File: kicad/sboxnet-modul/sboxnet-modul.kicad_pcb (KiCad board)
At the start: 2 copper layers, 67.3 x 62.2 mm, 38 parts, among them J1 Conn_01x03, J2 Conn_01x04, J4 8P8C, J5 8P8C, J6 sboxnet-buchse_2x17, SW1 SW_Push, U1 MCP1703A-3302_SOT223, U2 MCP1703A-5002_SOT223, U3 SN65HVD230, U4 ATxmega32A4U-AU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

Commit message: sboxnet modul v4
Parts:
- removed J2: Conn_01x04, Connector_PinHeader_2.54mm:PinHeader_1x04_P2.54mm_Vertical
- D4: value LED -> D4
- R1, R7: moved to F.Cu
- U4: value ATxmega32A4U-AU -> ATxmega64A4U-AU
- moved L1 4.02 mm to (100.5, 72.8)
- moved J1 3.70 mm to (146.9, 87.7), turned to 270 degrees
- moved R2 3.65 mm to (133.7, 127.9)
- moved R 2.57 mm to (91.5, 71.1)
- moved buchse 2.44 mm to (91.3, 128.3)
- moved J6 2.40 mm to (93.4, 122.9)
- moved C7 1.43 mm to (108.7, 72.8)
- moved R 0.11 mm to (151.1, 128.4)
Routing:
- net +V: track 67.2 -> 55.6 mm, vias 2 -> 0
- net Net-(R2-Pad2): track 2.49 -> 6.60 mm
- net AVCC: track 28.2 -> 32.3 mm
- net PD1: track 28.6 -> 24.6 mm
- net CANL: track 42.2 -> 39.0 mm
- net PB2: track 22.1 -> 19.1 mm
- net PB0: track 22.8 -> 19.9 mm
- net PB3: track 24.6 -> 21.7 mm
- net PC0: track 18.8 -> 16.0 mm
- net PD4: track 30.9 -> 28.2 mm
- net PA6: track 23.4 -> 20.7 mm
- net PA5: track 27.2 -> 24.7 mm
- net PC1: track 20.8 -> 18.3 mm
- net PD0: track 23.9 -> 21.4 mm
- net PA2: track 34.4 -> 31.9 mm
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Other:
- board size 67.3 x 62.2 mm -> 64.8 x 62.4 mm
- board text added: "(c) Thomas Maier tom@tom.ist-im-web.de 2021.01.19"
- board text added: "+7V"
- board text added: "+EXT"
- board text added: "or"
- board text added: "sboxnet modul v4"
- board text removed: "(c) Thomas Maier tom@tom.ist-im-web.de 2020.01.27"
- board text removed: "+V"
- board text removed: "ge"
- board text removed: "sboxnet modul v3"

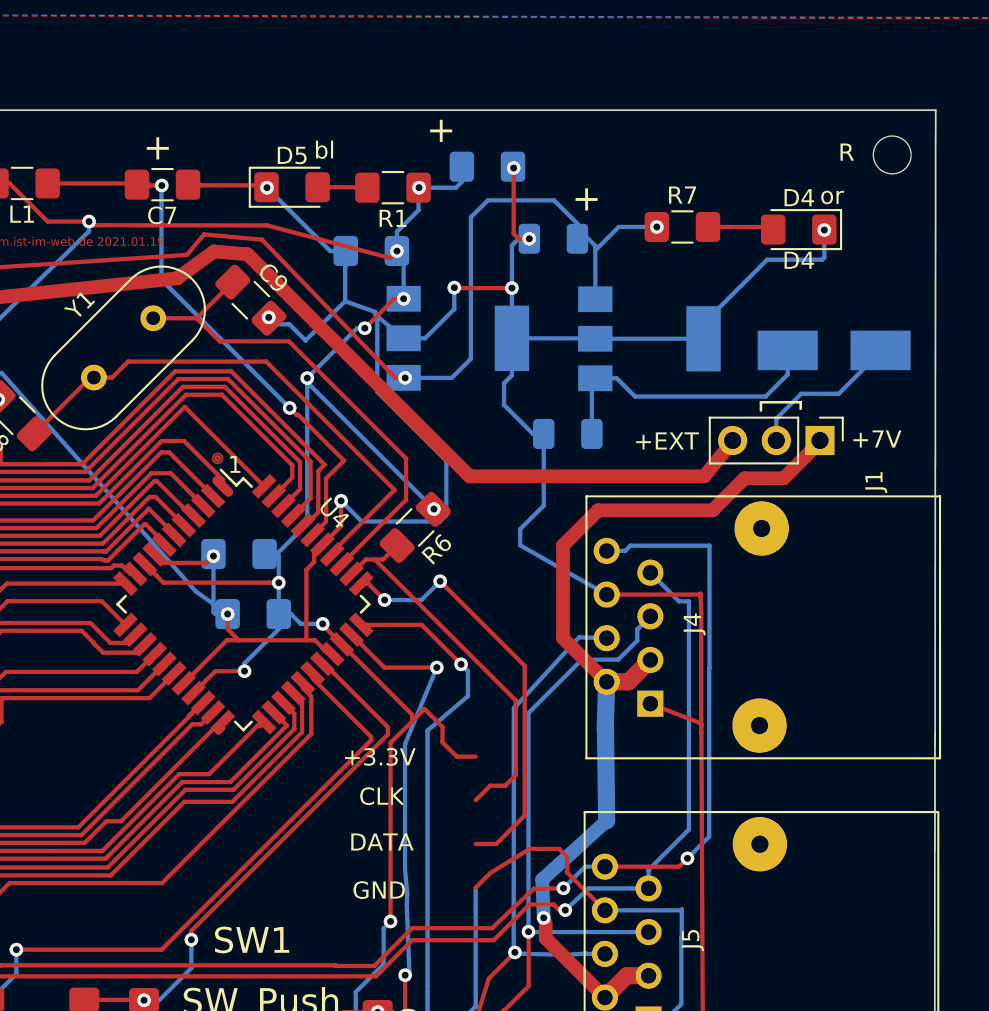
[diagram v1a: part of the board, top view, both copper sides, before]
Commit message: correct sboxnet-modul
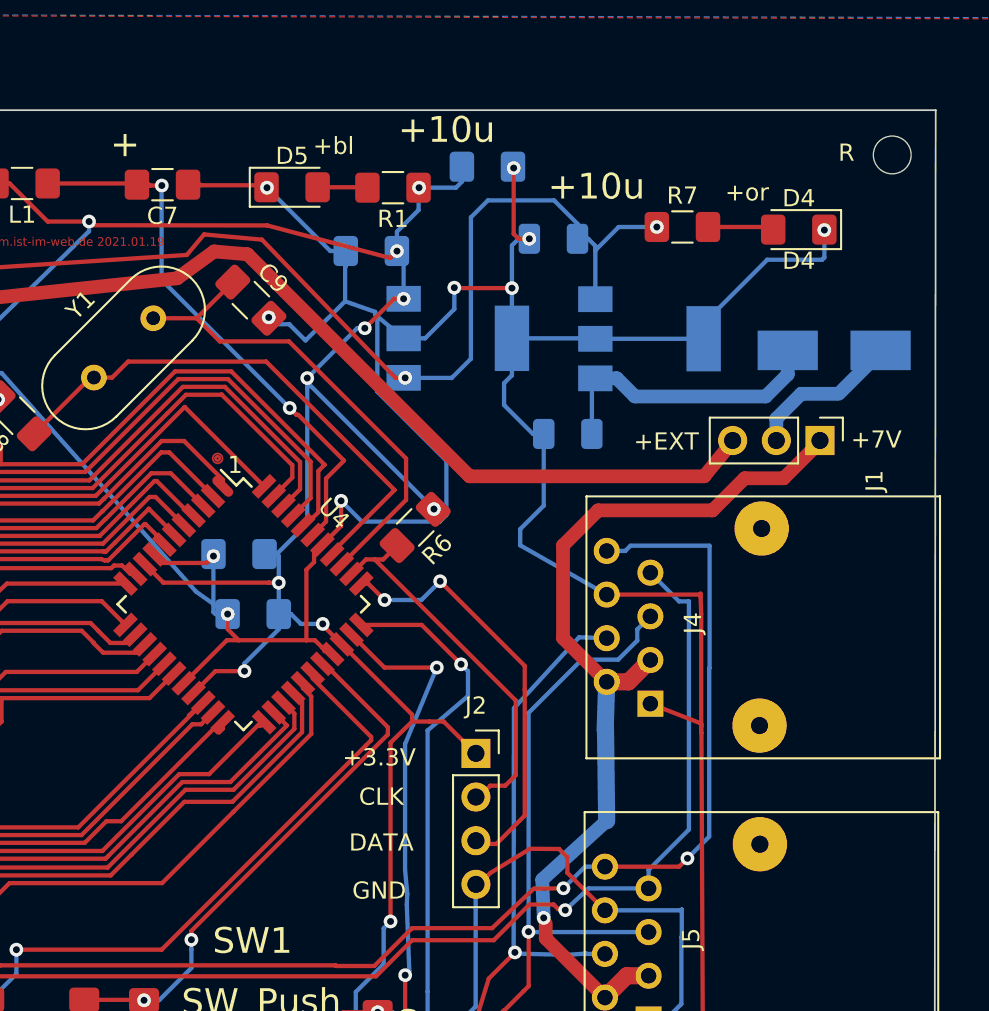
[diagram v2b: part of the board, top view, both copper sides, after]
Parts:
- added J2: Conn_01x04, Connector_PinSocket_2.54mm:PinSocket_1x04_P2.54mm_Vertical, F.Cu at (126.9, 105.9)
- U4: value ATxmega64A4U-AU -> ATxmega32A4U-AU
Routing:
- net +3V3: track 167.1 -> 165.9 mm
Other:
- board text added: "+10u"
- board text added: "+bl"
- board text added: "+or"
- board text removed: "bl"
- board text removed: "or"
